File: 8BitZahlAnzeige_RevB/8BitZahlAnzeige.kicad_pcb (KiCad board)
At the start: 2 copper layers, 208.3 x 137.2 mm, 77 parts, among them J1 USB4105-GF-A, J10 110-87-628-41-001101, J2 110-87-610-41-001101, J3 110-87-610-41-001101, J4 110-87-610-41-001101, J5 110-87-610-41-001101, J6 110-87-610-41-001101, J7 110-87-610-41-001101, J8 110-87-610-41-001101, J9 110-87-610-41-001101, SW1 SW_Push, SW2 SW_Push, SW3 SW_Push, SW4 SW_Push, SW5 SW_Push, SW6 SW_Push, SW7 SW_Push, SW8 SW_Push, SW9 SW_Push, U1 74HC165, U2 MAX7219, U3 74HC595

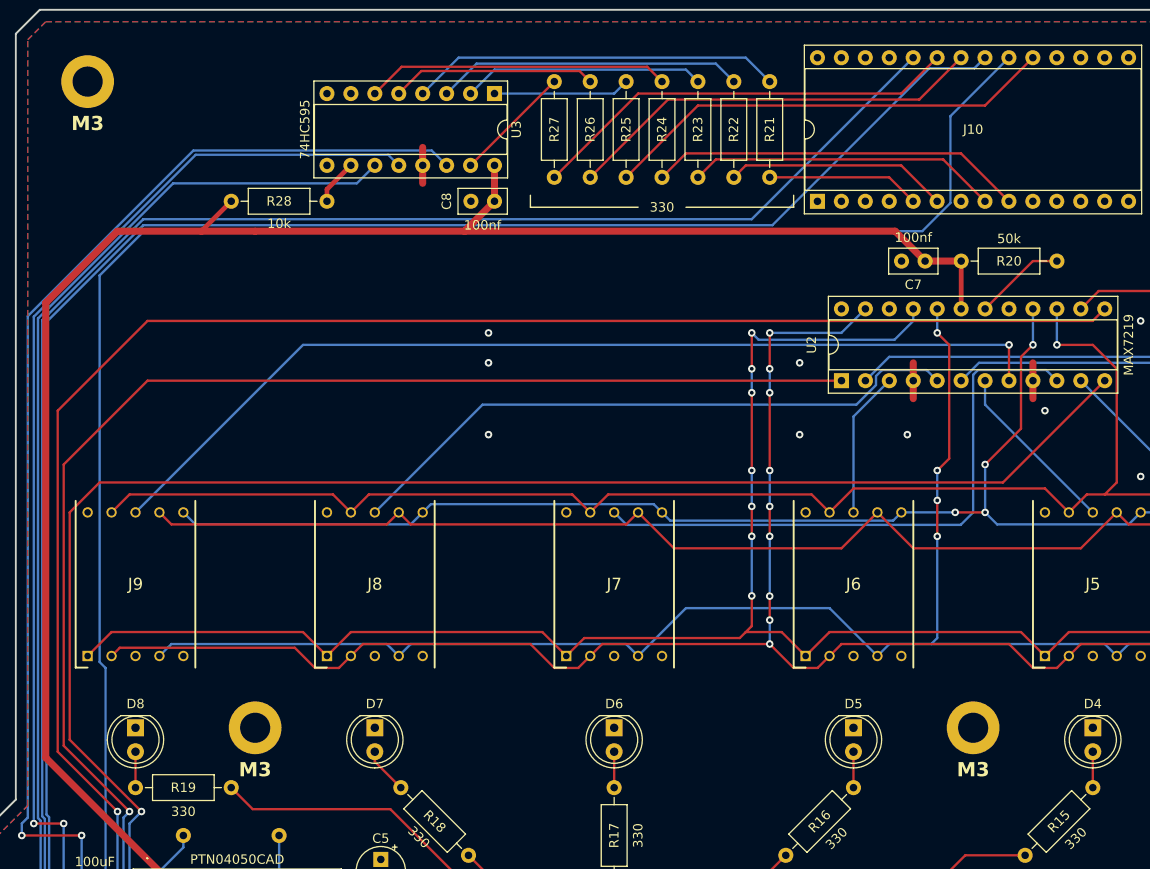
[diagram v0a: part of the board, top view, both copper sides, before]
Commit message: - Ignorieren automatisch generierter Backup-Ordner - Anpassen der Leitungen im Rev B Layout
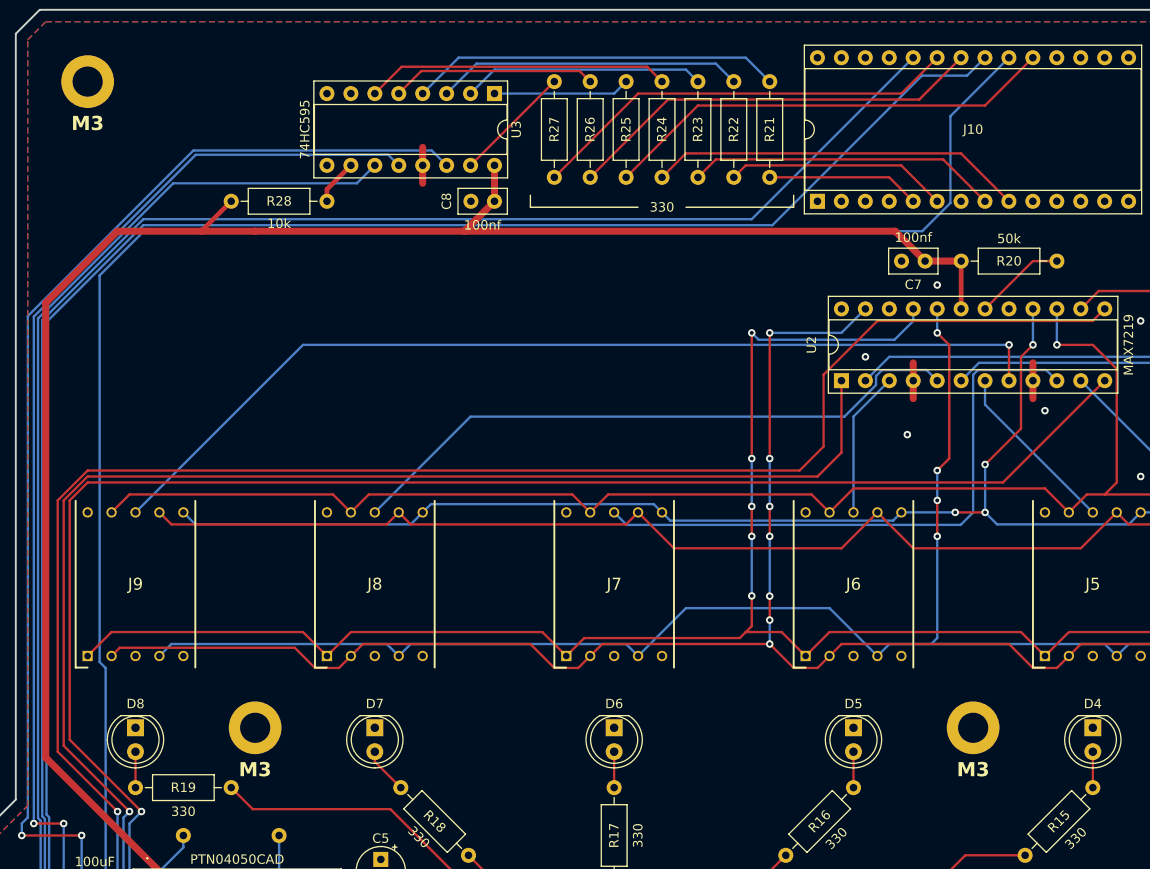
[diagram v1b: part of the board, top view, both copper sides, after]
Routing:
- net Net-(A1-D7): track 153.6 -> 155.9 mm
- net Net-(A1-D6): track 189.5 -> 188.4 mm
- net Net-(A1-D5): track 180.3 -> 181.1 mm
- net Net-(U2-SEG_E): vias 7 -> 5
- net Net-(U2-SEG_D): vias 9 -> 7
- net GNDREF: vias 14 -> 11
